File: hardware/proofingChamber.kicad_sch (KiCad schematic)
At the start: 14 parts, among them J1 SH1106 128x64 OLED (I2C inter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, J2 Conn_01x02, J3 Conn_01x02, SW1 RotaryEncoder_Switch, U1 ESP32-C3_SUPERMINI_TH, U2 DS18B20

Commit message: Refactor code structure for improved readability and maintainability
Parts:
- removed J1: SH1106 128x64 OLED (I2C interface), symbol Connector:Conn_01x04_Socket
- removed SW1: RotaryEncoder_Switch, symbol Device:RotaryEncoder_Switch
- added DS1: OLED_128X64_1.3_I2C, oled:LCD_OLED_128X64_1.3_I2C, symbol oled:OLED_128X64_1.3_I2C
- added J4: Conn_01x02, Connector_PinSocket_2.54mm:PinSocket_1x02_P2.54mm_Vertical, symbol Connector_Generic:Conn_01x02
- added SW2: RotaryEncoder_Switch_MP, Rotary_Encoder:RotaryEncoder_Alps_EC11E-Switch_Vertical_H20mm, symbol Device:RotaryEncoder_Switch_MP
- DCOOLING1: renamed from D2; footprint (none) -> LED_THT:LED_D3.0mm
- DCOOLING_RELAY1: renamed from D4; footprint (none) -> LED_THT:LED_D3.0mm
- DPROOFING1: renamed from D1; footprint (none) -> LED_THT:LED_D3.0mm
- DPROOFING_RELAY1: renamed from D3; footprint (none) -> LED_THT:LED_D3.0mm
- JCOOLING1: renamed from J3; footprint (none) -> Connector_PinSocket_2.54mm:PinSocket_1x02_P2.54mm_Vertical
- JPROOFING1: renamed from J2; footprint (none) -> Connector_PinSocket_2.54mm:PinSocket_1x02_P2.54mm_Vertical
- RCOOLING_LED1: renamed from R2; footprint (none) -> Resistor_THT:R_Axial_DIN0207_L6.3mm_D2.5mm_P7.62mm_Horizontal
- RCOOLING_RELAY_LED1: renamed from R4; footprint (none) -> Resistor_THT:R_Axial_DIN0207_L6.3mm_D2.5mm_P7.62mm_Horizontal
- RPROOFING_LED1: renamed from R1; footprint (none) -> Resistor_THT:R_Axial_DIN0207_L6.3mm_D2.5mm_P7.62mm_Horizontal
- RPROOFING_RELAY_LED1: renamed from R3; footprint (none) -> Resistor_THT:R_Axial_DIN0207_L6.3mm_D2.5mm_P7.62mm_Horizontal
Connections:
- net +5V: now also DS1.1 (VDD), J4.1 (5V)
- net COOLING_LED: now also U1.10 (GPIO10)
- net ENCODER_A: now also SW2.A
- net ENCODER_B: now also SW2.B
- net ENCODER_BTN: now also SW2.S2
- net GND: now also DS1.2 (GND), J4.2 (GND), SW2.C, SW2.MP, SW2.S1
- net PROOFING_LED: now also U1.6 (GPIO6)
- net SCK: now also DS1.3 (SCK)
- net SDA: now also DS1.4 (SDA)
- no-connect marks 0 -> 4

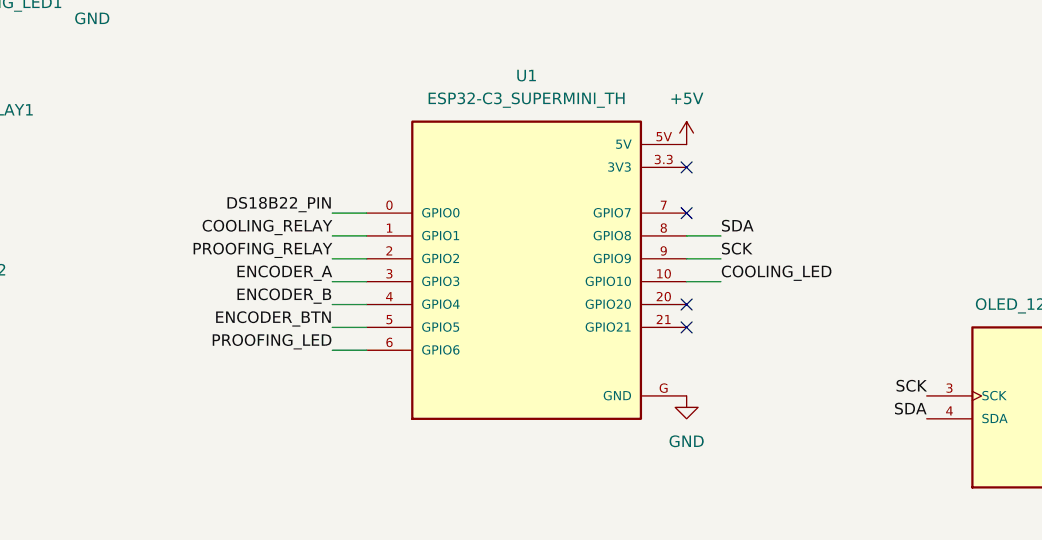
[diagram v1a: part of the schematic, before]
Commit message: Refactor hardware design files: remove obsolete proofingChamber.kicad_prl, update net classes and schematic connections
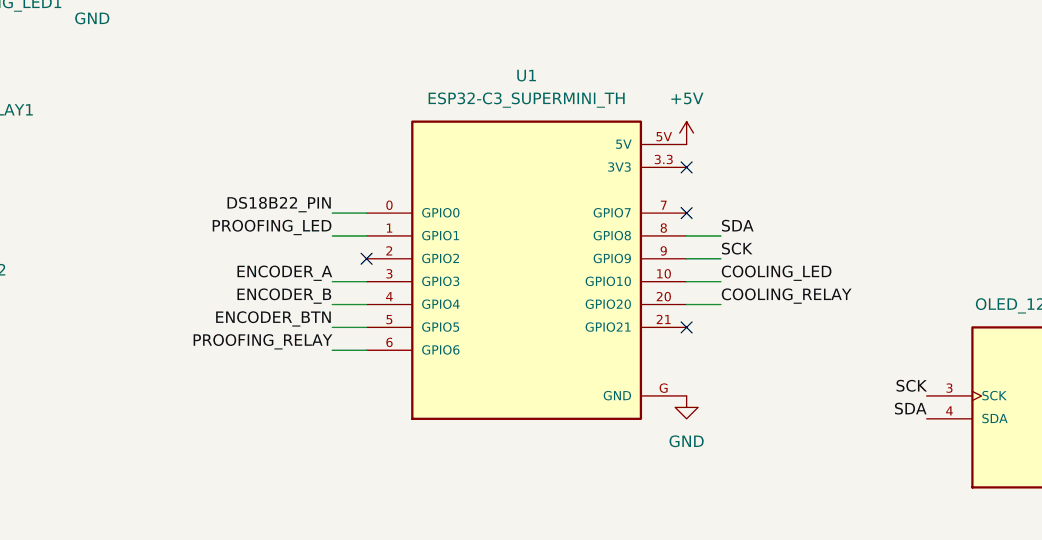
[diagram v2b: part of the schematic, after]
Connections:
- net COOLING_RELAY: now also U1.20 (GPIO20); no longer U1.1 (GPIO1)
- net PROOFING_LED: now also U1.1 (GPIO1); no longer U1.6 (GPIO6)
- net PROOFING_RELAY: now also U1.6 (GPIO6); no longer U1.2 (GPIO2)
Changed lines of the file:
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@@
 	)
 	(no_connect
-		(at 156.21 106.68)
+		(at 120.65 101.6)
 	)
 	(no_connect
@@
 	(wire
 		(pts
+			(xy 160.02 99.06) (xy 156.21 99.06)
+		)
+		(stroke
+			(width 0)
+			(type default)
+		)
+	)
+	(wire
+		(pts
+			(xy 201.93 39.37) (xy 219.71 39.37)
+		)
+		(stroke
+			(width 0)
+			(type default)
+		)
+	)
+	(wire
+		(pts
 			(xy 116.84 99.06) (xy 120.65 99.06)
 		)
@@
 	(wire
 		(pts
-			(xy 160.02 99.06) (xy 156.21 99.06)
-		)
-		(stroke
-			(width 0)
-			(type default)
-		)
-	)
-	(wire
-		(pts
-			(xy 201.93 39.37) (xy 219.71 39.37)
-		)
-		(stroke
-			(width 0)
-			(type default)
-		)
-	)
-	(wire
-		(pts
 			(xy 194.31 31.75) (xy 219.71 31.75)
 		)
@@
 	(wire
 		(pts
+			(xy 156.21 106.68) (xy 160.02 106.68)
+		)
+		(stroke
+			(width 0)
+			(type default)
+		)
+	)
+	(wire
+		(pts
 			(xy 116.84 104.14) (xy 120.65 104.14)
 		)
@@
 		(pts
 			(xy 55.88 100.33) (xy 62.23 100.33)
-		)
-		(stroke
-			(width 0)
-			(type default)
-		)
-	)
-	(wire
-		(pts
-			(xy 116.84 101.6) (xy 120.65 101.6)
 		)
 		(stroke
@@
 		)
 	)
-	(label "COOLING_RELAY"
-		(at 116.84 99.06 180)
-		(effects
-			(font
-				(size 1.27 1.27)
-			)
-			(justify right bottom)
-		)
-	)
 	(label "SDA"
 		(at 160.02 99.06 0)
@@
 		)
 	)
-	(label "PROOFING_LED"
-		(at 116.84 111.76 180)
-		(effects
-			(font
-				(size 1.27 1.27)
-			)
-			(justify right bottom)
-		)
-	)
 	(label "ENCODER_BTN"
 		(at 186.69 36.83 180)
@@
 		)
 	)
-	(label "PROOFING_RELAY"
-		(at 116.84 101.6 180)
-		(effects
-			(font
-				(size 1.27 1.27)
-			)
-			(justify right bottom)
-		)
-	)
 	(label "ENCODER_B"
 		(at 201.93 36.83 0)
@@
 	)
 	(label "COOLING_RELAY"
+		(at 160.02 106.68 0)
+		(effects
+			(font
+				(size 1.27 1.27)
+			)
+			(justify left bottom)
+		)
+	)
+	(label "PROOFING_RELAY"
+		(at 116.84 111.76 180)
+		(effects
+			(font
+				(size 1.27 1.27)
+			)
+			(justify right bottom)
+		)
+	)
+	(label "COOLING_RELAY"
 		(at 55.88 100.33 180)
 		(effects
@@
 		(effects
 			(font
+				(size 1.27 1.27)
+			)
+			(justify right bottom)
+		)
+	)
+	(label "PROOFING_LED"
+		(at 116.84 99.06 180)
+		(effects
+			(font

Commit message: Update PCB
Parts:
- removed DCOOLING_RELAY1, DPROOFING_RELAY1: LED, LED_THT:LED_D3.0mm, symbol Device:LED
- removed J4, JCOOLING1, JPROOFING1: Conn_01x02, Connector_PinSocket_2.54mm:PinSocket_1x02_P2.54mm_Vertical, symbol Connector_Generic:Conn_01x02
- removed RCOOLING_RELAY_LED1, RPROOFING_RELAY_LED1: R, Resistor_THT:R_Axial_DIN0207_L6.3mm_D2.5mm_P7.62mm_Horizontal, symbol Device:R
- removed U2: DS18B20, Package_TO_SOT_THT:TO-92_Inline, symbol Sensor_Temperature:DS18B20
- added J1: Conn_02x06_Odd_Even, Connector_PinSocket_2.54mm:PinSocket_2x06_P2.54mm_Horizontal, symbol Connector_Generic:Conn_02x06_Odd_Even
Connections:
- net +5V: now also J1.11 (Pin_11), J1.7 (Pin_7), J1.9 (Pin_9)
- net COOLING_LED: now also U1.21 (GPIO21); no longer U1.10 (GPIO10)
- net COOLING_RELAY: now also U1.2 (GPIO2), J1.3 (Pin_3); no longer U1.20 (GPIO20)
- net DS18B22_PIN: now also U1.20 (GPIO20), J1.1 (Pin_1); no longer U1.0 (GPIO0)
- net ENCODER_A: now also U1.7 (GPIO7); no longer U1.3 (GPIO3)
- net ENCODER_B: now also U1.6 (GPIO6); no longer U1.4 (GPIO4)
- net GND: now also J1.10 (Pin_10), J1.12 (Pin_12), J1.2 (Pin_2), J1.4 (Pin_4), J1.6 (Pin_6), J1.8 (Pin_8)
- net PROOFING_LED: now also U1.10 (GPIO10); no longer U1.1 (GPIO1)
- net PROOFING_RELAY: now also U1.1 (GPIO1), J1.5 (Pin_5); no longer U1.6 (GPIO6)
- no-connect marks 4 -> 1
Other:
- moved on the sheet: DCOOLING1, DPROOFING1, DS1, RCOOLING_LED1, RPROOFING_LED1, SW2
